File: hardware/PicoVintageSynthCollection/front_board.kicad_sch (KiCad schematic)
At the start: 29 parts, among them J3 from main board, J4 from main board, J8 panel jacks, SW1 EC11 SEL, SW2 EC11 A, SW3 EC11 B, SW4 RUN, SW5 BOOT

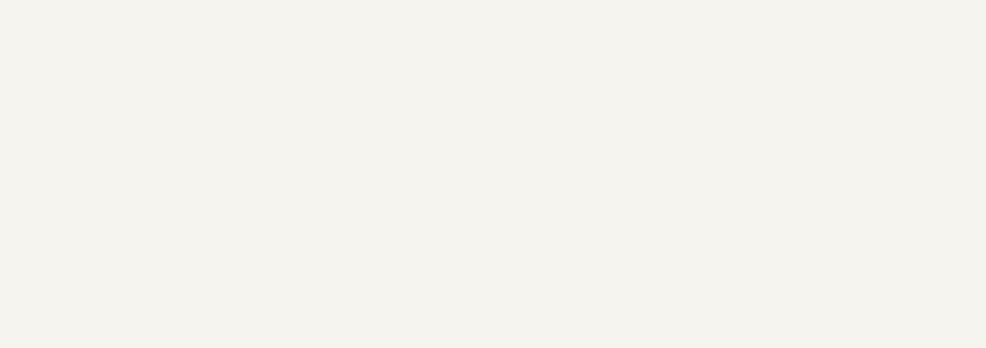
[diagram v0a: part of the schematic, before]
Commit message: Lay out the front board, where the panel has already decided everything
The main board layout was a series of choices. This one is mostly arithmetic:
the panel fixes where the three encoder shafts, the two buttons and the display
go, and the layout is what falls out. Board origin is panel (2.9, 14), so
SELECT lands at (22.5, 46.58), PARAM A and B at (10.0, 71.61) and (35.0, 71.61),
RUN and BOOT at (7.1, 46.58) and (37.9, 46.58). 229 track segments, 691 mm of
copper, 20 vias, ground poured both sides, DRC clean and in agreement with the
schematic.

What was actually decided:

J3 and J4 sit on the back at exactly the coordinates J1 and J2 occupy on the
main board. That works because both boards are drawn in the same frame -- each
has F.Cu facing the panel -- so a point on one is directly behind the same point
on the other and pin k meets pin k. It is the kind of thing that is obvious
until it is wrong, and wrong means a board that plugs together backwards.

J8 went to the back. On the panel side the encoder bodies fill the entire 6.5 mm
gap, so ten wires have no lane to reach the jacks below; behind the board they
run in the gap between the boards and leave at the bottom edge. For the same
reason its wires are soldered rather than plugged: a 2.54 mm header stands
8.5 mm tall and neither gap has room for one, let alone a housing on top of it.

The pull-ups and debounce footprints sit beside the encoder they serve, on the
back, where the encoders' courtyards do not reach because those are on the other
side of the board.

Both boards' lower standoffs moved from the corners to y 63. At y 77.5 the hole
lands inside the PARAM encoders' courtyards, which is a real DRC error rather
than a cosmetic one, and moving them cost a re-route of the main board -- hence
its board file changing here too. The front board is bolted to the panel by
three encoder nuts regardless.

One thing is not backed by a measurement, and it should be said plainly: DS1 is
drawn centred on the display mo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
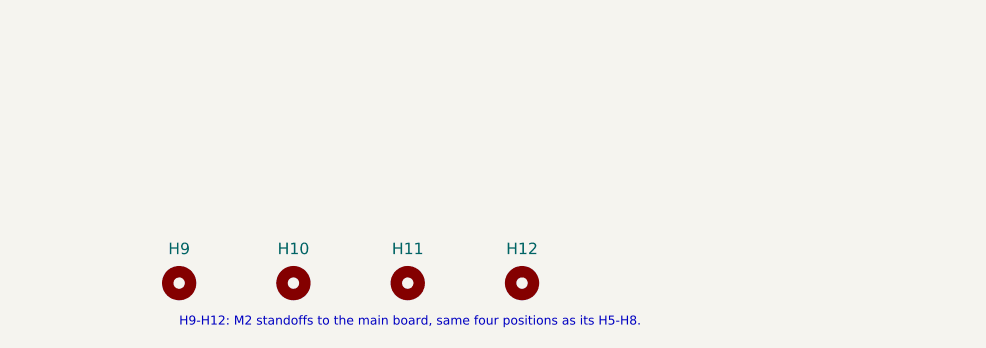
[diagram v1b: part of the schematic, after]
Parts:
- added H10, H11, H12, H9: M2 board standoff, MountingHole:MountingHole_2.2mm_M2, symbol Mechanical:MountingHole
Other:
- note added: "H9-H12: M2 standoffs to the main board, same four positions as its H5-H8."

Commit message: The display's pin 1 is VDD, not GND
Measured on the part now in hand: 1 VDD, 2 GND, 3 SCK, 4 SDA, numbered from the
display side with pin 1 on the left. The symbol had the order most modules use
-- GND, VCC, SCL, SDA -- so the board as drawn would have put 3.3 V on the
module's ground pin and ground on its supply. The display would not have
survived first power-up. The README has been warning about exactly this since
the schematic was drawn ("some vendors swap the first two"); it turns out this
vendor is one of them.

The fix is two pins swapped in the symbol and the two power symbols exchanged in
the sheet, which changes the netlist, so the front board is re-routed: 230
segments, 19 vias, still no failures. The header position needed no change --
it is centred on the module and the module is centred on the board, so DS1 was
already where it belongs, with pin 1 on the left.

Also carried across while the boards were open: DNP and exclude-from-BOM now
travel from the symbols to the footprints, so schematic parity is clean rather
than clean-if-you-only-look-at-errors.

Still assumed, and now the only thing that is: the display's four mounting holes
at 30 x 28 mm. They are non-plated and carry nothing, so being wrong costs a
standoff rather than a board, but they have not been measured.

Co-Authored-By: Claude Fable 5 <noreply@anthropic.com>
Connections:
- net +3V3: now also DS1.1 (VDD); no longer DS1.2 (VCC)
- net GND: now also DS1.2 (GND); no longer DS1.1 (GND)
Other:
- note added: "OLED: I2C1 at 1 MHz, u8g2 SH1106 driver, address 0x3C. Pin order measured on the part in hand: 1 VDD, 2 GND, 3 SCK, 4 SDA, numbered from the display side with pin 1 on the left. The usual GND-VCC-SCL-SDA order would have put 3V3 on the module's ground pin. Header is centred on the module; the four M2 holes are still assumed. Modules carry their own SDA/SCL pull-ups (~4k7)."
- note removed: "OLED: I2C1 at 1 MHz, u8g2 SH1106 driver, address 0x3C. Modules carry their own SDA/SCL pull-ups (~4k7). Pin order GND-VCC-SCL-SDA is the common one - check the module, some vendors swap the first two. Panel window is cut to the pixels (active area starts 7.35 mm below the module top edge)."
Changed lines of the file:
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@@
 		)
 	)
-	(text "OLED: I2C1 at 1 MHz, u8g2 SH1106 driver, address 0x3C.\nModules carry their own SDA/SCL pull-ups (~4k7).\nPin order GND-VCC-SCL-SDA is the common one - check the\nmodule, some vendors swap the first two.\nPanel window is cut to the pixels (active area starts\n7.35 mm below the module top edge)."
+	(text "OLED: I2C1 at 1 MHz, u8g2 SH1106 driver, address 0x3C.\nPin order measured on the part in hand: 1 VDD, 2 GND, 3 SCK, 4 SDA,\nnumbered from the display side with pin 1 on the left. The usual\nGND-VCC-SCL-SDA order would have put 3V3 on the module's ground pin.\nHeader is centred on the module; the four M2 holes are still assumed.\nModules carry their own SDA/SCL pull-ups (~4k7)."
 		(exclude_from_sim no)
 		(at 218.44 81.28 0)
@@
 	(symbol
 		(lib_id "power:GND")
-		(at 227.33 62.23 270)
+		(at 227.33 64.77 270)
 		(unit 1)
 		(body_style 1)
@@
 		(dnp no)
 		(property "Reference" "#PWR057"
-			(at 224.155 63.5 90)
+			(at 224.155 66.04 90)
 			(show_name no)
 			(do_not_autoplace no)
@@
 		)
 		(property "Value" "GND"
-			(at 224.155 62.23 90)
+			(at 224.155 64.77 90)
 			(show_name no)
 			(do_not_autoplace no)
@@
 		)
 		(property "Footprint" ""
-			(at 227.33 62.23 0)
+			(at 227.33 64.77 0)
 			(show_name no)
 			(do_not_autoplace no)
@@
 		)
 		(property "Datasheet" ""
-			(at 227.33 62.23 0)
+			(at 227.33 64.77 0)
 			(show_name no)
 			(do_not_autoplace no)
@@
 		)
 		(property "Description" ""
-			(at 227.33 62.23 0)
+			(at 227.33 64.77 0)
 			(show_name no)
 			(do_not_autoplace no)
@@
 	(symbol
 		(lib_id "power:+3V3")
-		(at 227.33 64.77 90)
+		(at 227.33 62.23 90)
 		(unit 1)
 		(body_style 1)
@@
 		(dnp no)
 		(property "Reference" "#PWR058"
-			(at 224.155 66.04 90)
+			(at 224.155 63.5 90)
 			(show_name no)
 			(do_not_autoplace no)
@@
 		)
 		(property "Value" "+3V3"
-			(at 224.155 64.77 90)
+			(at 224.155 62.23 90)
 			(show_name no)
 			(do_not_autoplace no)
@@
 		)
 		(property "Footprint" ""
-			(at 227.33 64.77 0)
+			(at 227.33 62.23 0)
 			(show_name no)
 			(do_not_autoplace no)
@@
 		)
 		(property "Datasheet" ""
-			(at 227.33 64.77 0)
+			(at 227.33 62.23 0)
 			(show_name no)
 			(do_not_autoplace no)
@@
 		)
 		(property "Description" ""
-			(at 227.33 64.77 0)
+			(at 227.33 62.23 0)
 			(show_name no)
 			(do_not_autoplace no)
